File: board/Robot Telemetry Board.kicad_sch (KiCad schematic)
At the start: 29 parts, among them J5 Conn_01x04, J6 Conn_01x02, J7 Conn_01x02, U1 Teensy4.1, U10 ADXL372

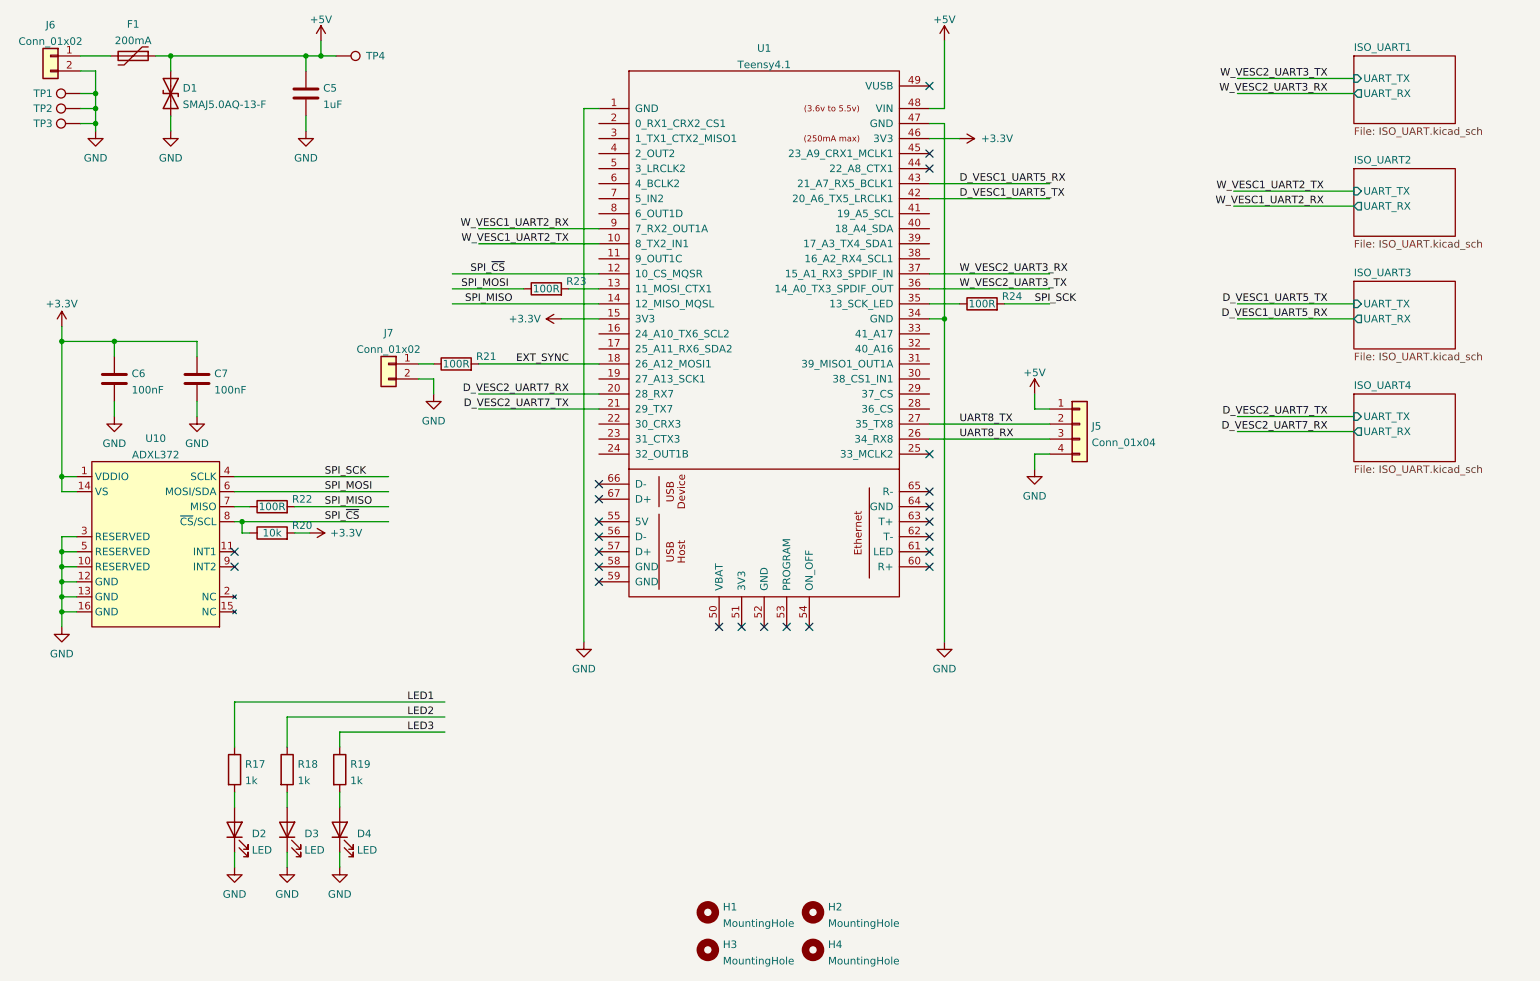
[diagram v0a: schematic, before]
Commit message: Completing the top half
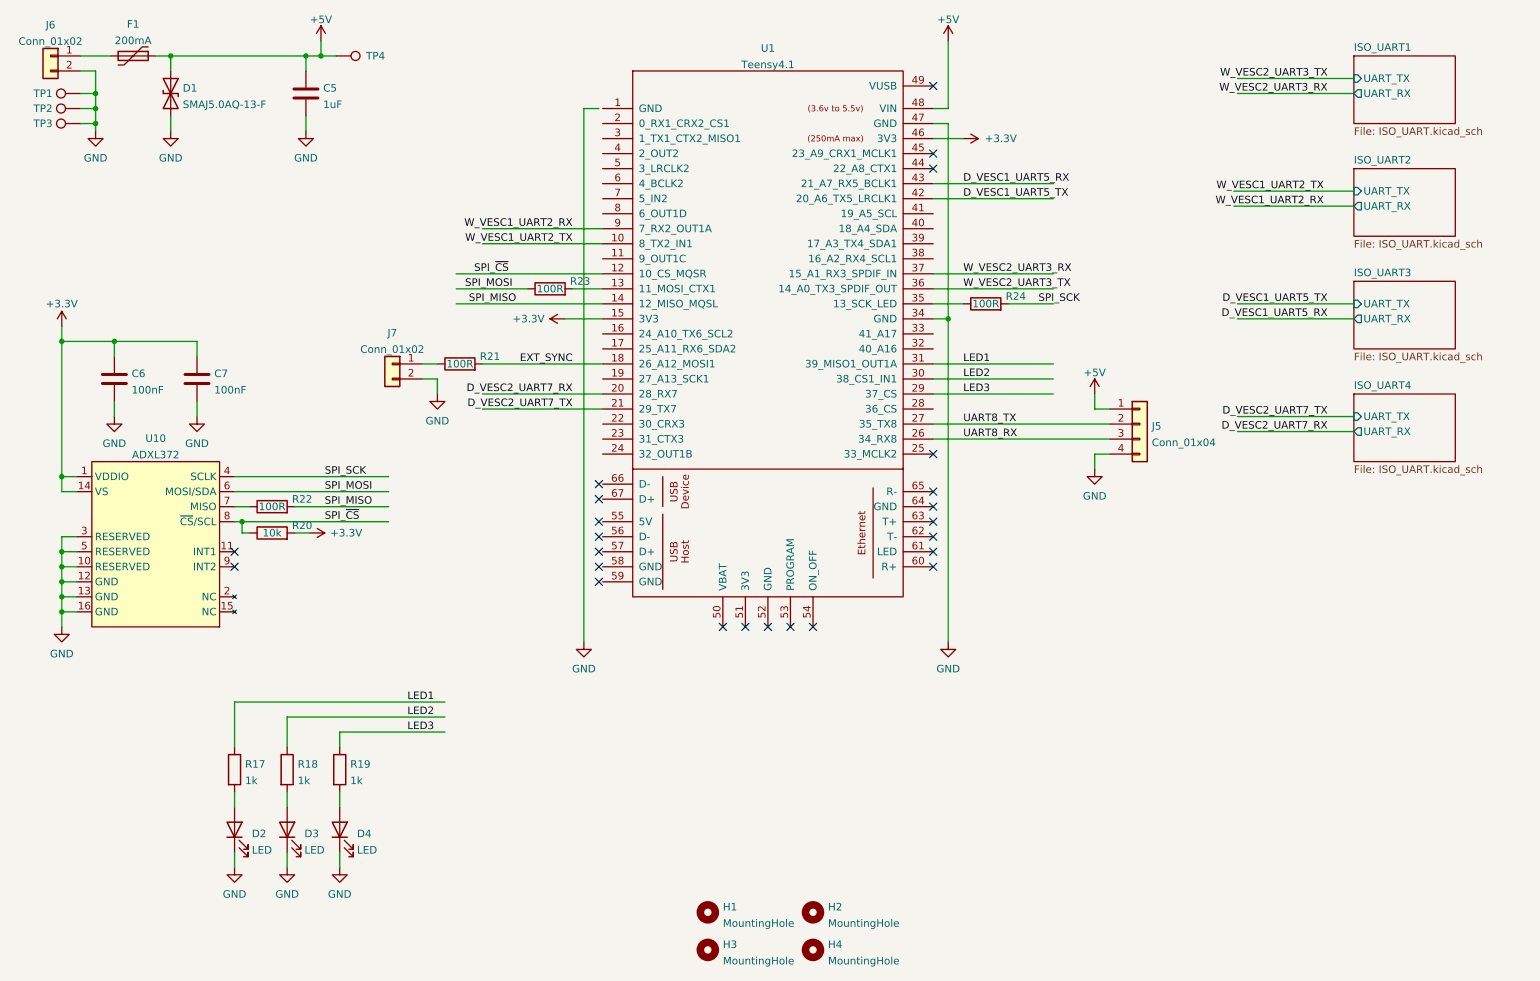
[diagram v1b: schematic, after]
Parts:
- U1: footprint teensy:Teensy41 -> teensy:Teensy41_DIP
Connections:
- net GND: no longer U1.1 (GND)
- net LED1: now also U1.31 (39_MISO1_OUT1A)
- net LED2: now also U1.30 (38_CS1_IN1)
- net LED3: now also U1.29 (37_CS)
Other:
- moved on the sheet: J5, J7, R21, R23, R24, U1

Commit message: Adding LCSC part numbers
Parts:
- C5: LCSC (none) -> C15849
- C6, C7: LCSC (none) -> C14663
- F1: LCSC (none) -> C207011
- J5: LCSC (none) -> C131334
- J6, J7: LCSC (none) -> C173752
- R17, R18, R19: LCSC (none) -> C21190
- R20: LCSC (none) -> C25804
- R21, R22, R23, R24: LCSC (none) -> C22775
- U10: LCSC (none) -> C579465
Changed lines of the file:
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@@
+      (effects (font (size 1.27 1.27)) hide)
+    )
+    (property "LCSC" "~" (id 4) (at 32.385 46.99 0)
       (effects (font (size 1.27 1.27)) hide)
     )
@@
       (effects (font (size 1.27 1.27)) hide)
     )
+    (property "LCSC" "~" (id 4) (at 75.565 38.1 0)
+      (effects (font (size 1.27 1.27)) hide)
+    )
     (pin "1")
   )
@@
     )
     (property "Datasheet" "~" (id 3) (at 38.1 92.71 0)
+      (effects (font (size 1.27 1.27)) hide)
+    )
+    (property "LCSC" "C14663" (id 4) (at 38.1 92.71 0)
       (effects (font (size 1.27 1.27)) hide)
     )
@@
       (effects (font (size 1.27 1.27)) hide)
     )
+    (property "LCSC" "C25804" (id 4) (at 64.77 118.745 0)
+      (effects (font (size 1.27 1.27)) hide)
+    )
     (pin "1")
     (pin "2")
@@
     )
     (property "Datasheet" "~" (id 3) (at 58.42 158.75 0)
+      (effects (font (size 1.27 1.27)) hide)
+    )
+    (property "LCSC" "C21190" (id 4) (at 58.42 158.75 0)
       (effects (font (size 1.27 1.27)) hide)
     )
@@
     )
     (property "Datasheet" "~" (id 3) (at 76.2 158.75 0)
+      (effects (font (size 1.27 1.27)) hide)
+    )
+    (property "LCSC" "C21190" (id 4) (at 76.2 158.75 0)
       (effects (font (size 1.27 1.27)) hide)
     )
@@
       (effects (font (size 1.27 1.27)) hide)
     )
+    (property "LCSC" "C22775" (id 4) (at 111.76 77.47 0)
+      (effects (font (size 1.27 1.27)) hide)
+    )
     (pin "1")
     (pin "2")
@@
       (effects (font (size 1.27 1.27)) hide)
     )
+    (property "LCSC" "C21190" (id 4) (at 67.31 158.75 0)
+      (effects (font (size 1.27 1.27)) hide)
+    )
     (pin "1")
     (pin "2")
@@
     )
     (property "Datasheet" "~" (id 3) (at 52.07 92.71 0)
+      (effects (font (size 1.27 1.27)) hide)
+    )
+    (property "LCSC" "C14663" (id 4) (at 52.07 92.71 0)
       (effects (font (size 1.27 1.27)) hide)
     )
@@
       (effects (font (size 1.27 1.27)) hide)
     )
+    (property "LCSC" "C173752" (id 4) (at 27.305 38.1 0)
+      (effects (font (size 1.27 1.27)) hide)
+    )
     (pin "1")
     (pin "2")
@@
     )
     (property "Datasheet" "~" (id 3) (at 211.455 100.33 0)
+      (effects (font (size 1.27 1.27)) hide)
+    )
+    (property "LCSC" "C131334" (id 4) (at 211.455 100.33 0)
       (effects (font (size 1.27 1.27)) hide)
     )
@@
     )
     (property "Datasheet" "" (id 3) (at 55.88 106.68 0)
+      (effects (font (size 1.27 1.27)) hide)
+    )
+    (property "LCSC" "C579465" (id 4) (at 55.88 106.68 0)
       (effects (font (size 1.27 1.27)) hide)
     )
@@
       (effects (font (size 1.27 1.27)) hide)
     )
+    (property "LCSC" "C207011" (id 5) (at 41.275 38.1 0)
+      (effects (font (size 1.27 1.27)) hide)
+    )
     (pin "1")
     (pin "2")
@@
       (effects (font (size 1.27 1.27)) hide)
     )
+    (property "LCSC" "C173752" (id 4) (at 85.09 90.17 0)
+      (effects (font (size 1.27 1.27)) hide)
+    )
     (pin "1")
     (pin "2")
@@
       (effects (font (size 1.27 1.27)) hide)
     )
+    (property "LCSC" "C22775" (id 4) (at 185.42 80.01 0)
+      (effects (font (size 1.27 1.27)) hide)
+    )
     (pin "1")
     (pin "2")
@@
       (effects (font (size 1.27 1.27)) hide)
     )
+    (property "LCSC" "~" (id 4) (at 32.385 49.53 0)
+      (effects (font (size 1.27 1.27)) hide)
+    )
     (pin "1")
   )
@@
     )
     (property "Datasheet" "~" (id 3) (at 32.385 49.53 0)
+      (effects (font (size 1.27 1.27)) hide)
+    )
+    (property "LCSC" "~" (id 4) (at 32.385 44.45 0)
       (effects (font (size 1.27 1.27)) hide)
     )
@@
       (effects (font (size 1.27 1.27)) hide)
     )
+    (property "LCSC" "C22775" (id 4) (at 96.52 90.17 0)
+      (effects (font (size 1.27 1.27)) hide)
+    )
     (pin "1")
     (pin "2")
@@
     )
     (property "Datasheet" "~" (id 3) (at 70.485 44.45 0)
+      (effects (font (size 1.27 1.27)) hide)
+    )
+    (property "LCSC" "C15849" (id 4) (at 70.485 44.45 0)
       (effects (font (size 1.27 1.27)) hide)
     )
@@
       (effects (font (size 1.27 1.27)) hide)
     )
+    (property "LCSC" "C22775" (id 4) (at 64.77 114.3 0)
+      (effects (font (size 1.27 1.27)) hide)
+    )
